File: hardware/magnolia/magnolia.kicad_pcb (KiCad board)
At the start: 4 copper layers, 70.7 x 53.3 mm, 7 parts, among them J1 NEIGHBOR1, J2 NEIGHBOR2, J7 BONUS_ROW

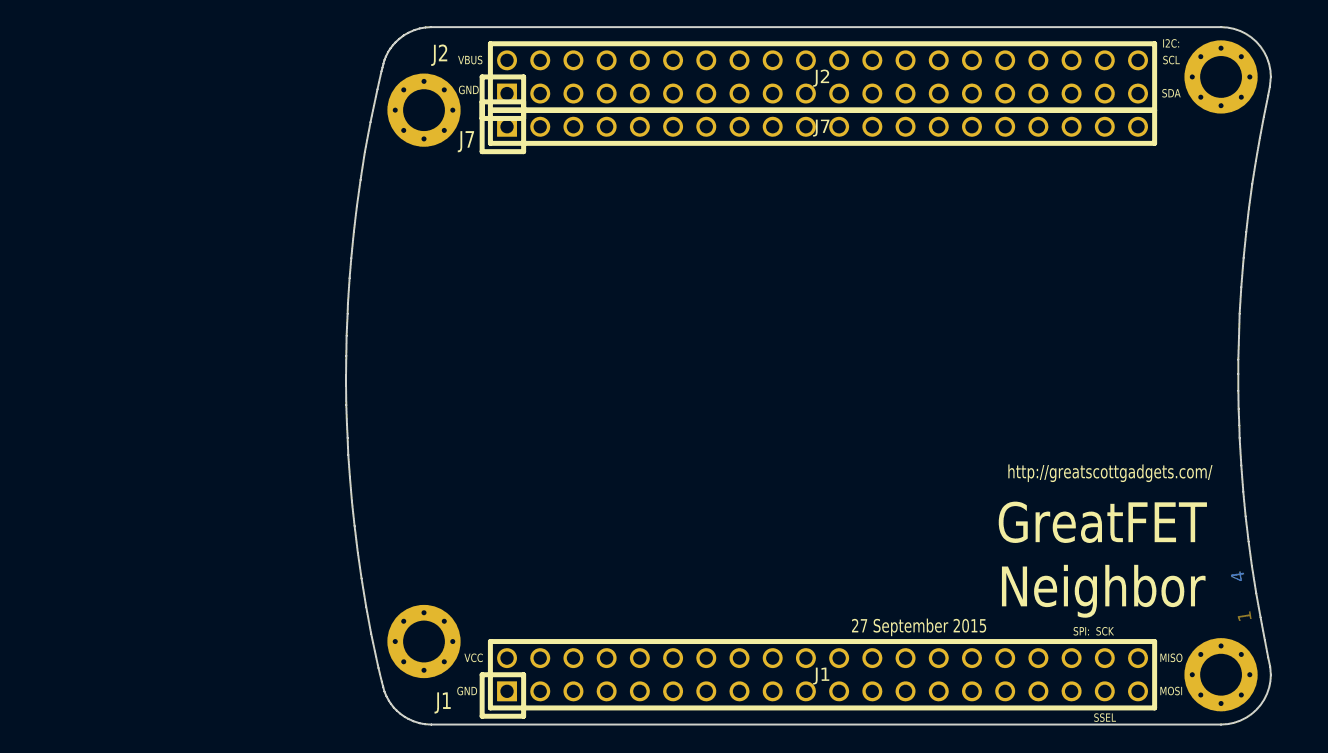
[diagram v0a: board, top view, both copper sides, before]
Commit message: magnolia: route more of Magnolia
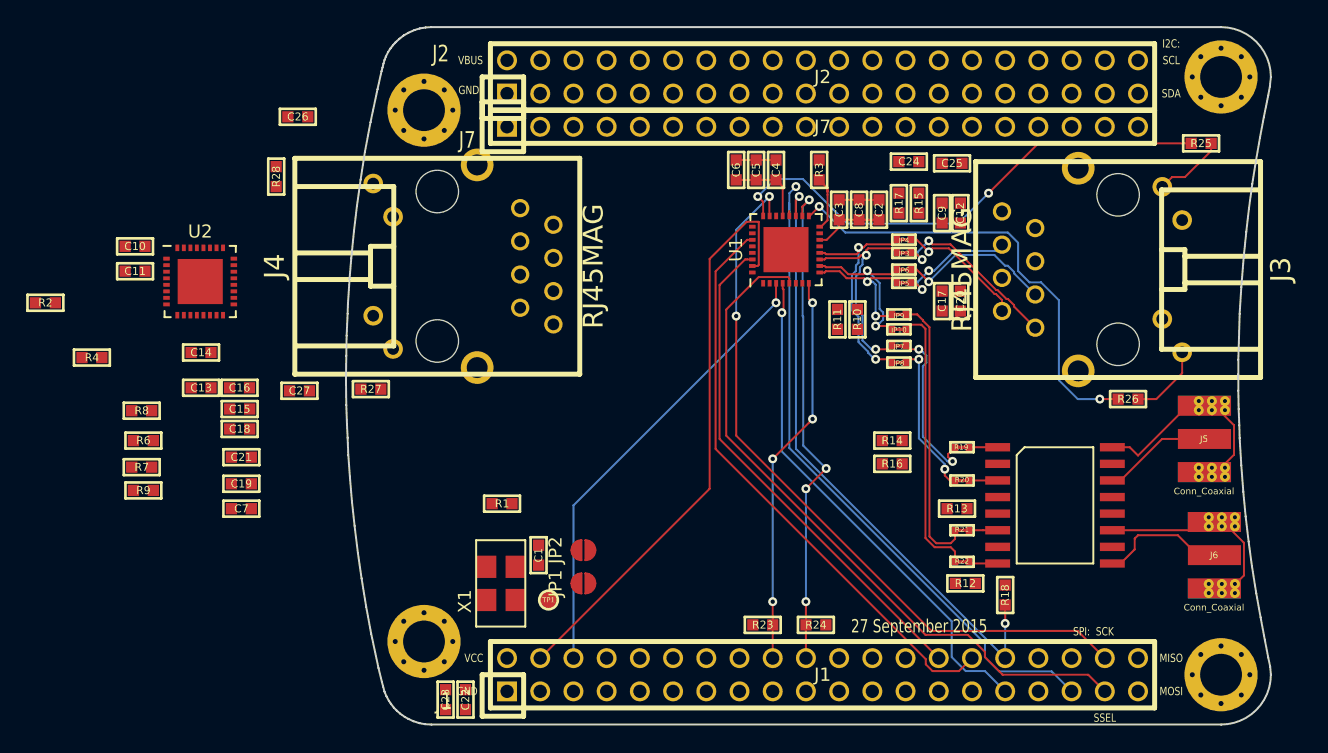
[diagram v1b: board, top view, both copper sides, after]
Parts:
- added C1: 10nF, gsg-modules:0603, F.Cu at (124.3, 109.0)
- added C10: 100nF, gsg-modules:0603, F.Cu at (93.5, 85.3)
- added C11: 1uF, gsg-modules:0603, F.Cu at (93.5, 87.2)
- added C12: 0.1uF, gsg-modules:0603, F.Cu at (156.6, 82.8)
- added C13: 10nF, gsg-modules:0603, F.Cu at (98.5, 96.2)
- added C14: 0.1uF, gsg-modules:0603, F.Cu at (98.5, 93.5)
- added C15: 1uF, gsg-modules:0603, F.Cu at (101.5, 97.8)
- added C16: 100nF, gsg-modules:0603, F.Cu at (101.5, 96.2)
- added C17: 1uF, gsg-modules:0603, F.Cu at (155.2, 89.5)
- added C18: 1uF, gsg-modules:0603, F.Cu at (101.5, 99.3)
- added C19: 1uF, gsg-modules:0603, F.Cu at (101.6, 103.5)
- added C2: 10nF, gsg-modules:0603, F.Cu at (150.4, 82.5)
- added C20: 0.1uF, gsg-modules:0603, F.Cu at (156.6, 89.5)
- added C21: 0.1uF, gsg-modules:0603, F.Cu at (101.6, 101.5)
- added C22: CP, gsg-modules:0603, F.Cu at (118.7, 120.0)
- added C23: CP, gsg-modules:0603, F.Cu at (117.2, 120.0)
- added C24: 100nF, gsg-modules:0603, F.Cu at (152.7, 78.9)
- added C25: 100nF, gsg-modules:0603, F.Cu at (156.0, 79.0)
- added C26: 100nF, gsg-modules:0603, F.Cu at (105.9, 75.4)
- added C27: 100nF, gsg-modules:0603, F.Cu at (106.0, 96.4)
- added C3: 100nF, gsg-modules:0603, F.Cu at (147.3, 82.5)
- added C4: 10nF, gsg-modules:0603, F.Cu at (142.5, 79.5)
- added C5: 1uF, gsg-modules:0603, F.Cu at (141.0, 79.5)
- added C6: 100nF, gsg-modules:0603, F.Cu at (139.4, 79.5)
- added C7: 10nF, gsg-modules:0603, F.Cu at (101.6, 105.4)
- added C8: 1uF, gsg-modules:0603, F.Cu at (148.8, 82.5)
- added C9: 1uF, gsg-modules:0603, F.Cu at (155.2, 82.8)
- added J3: RJ45MAG, gsg-modules:rj45-wiznet-rb1-125bag1a, F.Cu at (168.7, 87.1)
- added J4: RJ45MAG, gsg-modules:rj45-wiznet-rb1-125bag1a, F.Cu at (116.6, 86.9)
- added J5: Conn_Coaxial, gsg-modules:SMA-EDGE, F.Cu at (173.2, 100.1)
- added J6: Conn_Coaxial, gsg-modules:SMA-EDGE, F.Cu at (174.0, 109.0)
- added JP1: Jumper, conn-test:JUMPER-SOLDER-SMD, F.Cu at (127.8, 111.1)
- added JP10: Jumper_NC_Small, gsg-modules:0402-SHORT-10MIL, F.Cu at (151.9, 91.7)
- added JP2: Jumper, conn-test:JUMPER-SOLDER-SMD, F.Cu at (127.8, 108.6)
- added JP3: Jumper_NC_Small, gsg-modules:0402-SHORT-10MIL, F.Cu at (152.3, 85.9)
- added JP4: Jumper_NC_Small, gsg-modules:0402-SHORT-10MIL, F.Cu at (152.3, 84.8)
- added JP5: Jumper_NC_Small, gsg-modules:0402-SHORT-10MIL, F.Cu at (152.3, 88.1)
- added JP6: Jumper_NC_Small, gsg-modules:0402-SHORT-10MIL, F.Cu at (152.3, 87.1)
- added JP7: Jumper_NC_Small, gsg-modules:0402-SHORT-10MIL, F.Cu at (151.9, 93.0)
- added JP8: Jumper_NC_Small, gsg-modules:0402-SHORT-10MIL, F.Cu at (151.9, 94.2)
- added JP9: Jumper_NC_Small, gsg-modules:0402-SHORT-10MIL, F.Cu at (151.9, 90.6)
- added R1: 10K, gsg-modules:0603, F.Cu at (121.5, 105.0)
- added R10: 49R9, gsg-modules:0603, F.Cu at (148.7, 90.9)
- added R11: 49R9, gsg-modules:0603, F.Cu at (147.2, 90.9)
- added R12: 0R, gsg-modules:0603, F.Cu at (157.0, 111.1)
- added R13: 0R, gsg-modules:0603, F.Cu at (156.3, 105.4)
- added R14: 0R, gsg-modules:0603, F.Cu at (151.4, 100.2)
- added R15: 49R9, gsg-modules:0603, F.Cu at (153.4, 82.0)
- added R16: 0R, gsg-modules:0603, F.Cu at (151.4, 102.0)
- added R17: 49R9, gsg-modules:0603, F.Cu at (151.9, 82.0)
- added R18: 2K2, gsg-modules:0603, F.Cu at (160.0, 112.0)
- added R19: R-SHORTED, gsg-modules:0402-SHORT-10MIL, F.Cu at (156.7, 100.7)
- added R2: 2K49, gsg-modules:0603, F.Cu at (86.6, 89.7)
- added R20: R-SHORTED, gsg-modules:0402-SHORT-10MIL, F.Cu at (156.7, 103.3)
- added R21: R-SHORTED, gsg-modules:0402-SHORT-10MIL, F.Cu at (156.7, 107.1)
- added R22: R-SHORTED, gsg-modules:0402-SHORT-10MIL, F.Cu at (156.7, 109.5)
- added R23: 10K, gsg-modules:0603, F.Cu at (141.5, 114.3)
- added R24: 10K, gsg-modules:0603, F.Cu at (145.5, 114.3)
- added R25: 1K, gsg-modules:0603, F.Cu at (175.0, 77.5)
- added R26: 1K, gsg-modules:0603, F.Cu at (169.4, 97.0)
- added R27: 1K, gsg-modules:0603, F.Cu at (111.5, 96.3)
- added R28: 1K, gsg-modules:0603, F.Cu at (104.3, 80.0)
- added R3: 4K87 +/- 1%, gsg-modules:0603, F.Cu at (145.8, 79.5)
- added R4: 4K87 +/- 1%, gsg-modules:0603, F.Cu at (90.2, 93.9)
- added R6: 49R9, gsg-modules:0603, F.Cu at (94.1, 100.2)
- added R7: 49R9, gsg-modules:0603, F.Cu at (94.0, 102.2)
- added R8: 49R9, gsg-modules:0603, F.Cu at (94.0, 97.9)
- added R9: 49R9, gsg-modules:0603, F.Cu at (94.1, 104.0)
- added T1: 749010012A, gsg-modules:749010012A, F.Cu at (163.8, 105.2)
- added TP1: Test_Point, gsg-modules:TESTPOINT-50MIL, F.Cu at (125.1, 112.4)
- added U1: DP83822, gsg-modules:QFN-32_EP_5.15x5.15_Pitch0.5mm, F.Cu at (143.3, 85.6)
- added U2: DP83822, gsg-modules:QFN-32_EP_5.15x5.15_Pitch0.5mm, F.Cu at (98.5, 88.0)
- added X1: ASFL1, gsg-modules:ASFL1, F.Cu at (122.6, 109.9)
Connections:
- net VCC renamed +3V3
- J1 pad 10: (no net) -> /P1_1
- J1 pad 11: (no net) -> /CLK0
- J1 pad 12: (no net) -> /P1_2
- J1 pad 13: (no net) -> /P1_5
- J1 pad 14: (no net) -> /P5_2
- J1 pad 15: (no net) -> /P1_7
- J1 pad 16: (no net) -> /P1_6
- J1 pad 17: (no net) -> /P1_9
- J1 pad 18: (no net) -> /INT_PWDN
- J1 pad 19: (no net) -> /P5_3
- J1 pad 20: (no net) -> /PHY_RESET
- J1 pad 21: (no net) -> /P1_12
- J1 pad 22: (no net) -> /P1_11
- J1 pad 23: (no net) -> /P5_5
- J1 pad 24: (no net) -> /P5_4
- J1 pad 25: (no net) -> /P1_14
- J1 pad 26: (no net) -> /P1_13
- J1 pad 27: (no net) -> /P5_6
- J1 pad 28: (no net) -> /MII_RX_D0
- J1 pad 29: (no net) -> /P5_7
- J1 pad 3: (no net) -> /P4_9
- J1 pad 30: (no net) -> /MII_CRS_DV
- J1 pad 31: (no net) -> /MII_TX_D0
- J1 pad 32: (no net) -> /SMI_MDIO
- J1 pad 33: (no net) -> /P9_5
- J1 pad 34: (no net) -> /P9_6
- J1 pad 35: (no net) -> /SMI_MDC
- J1 pad 36: (no net) -> /P6_0
- J1 pad 37: (no net) -> /MII_TX_D1
- J1 pad 38: (no net) -> /ENET1_RMII_CLK
- J1 pad 39: (no net) -> /P1_4
- J1 pad 4: (no net) -> /MII_RX_D1
- J1 pad 40: (no net) -> /P1_3
- J1 pad 5: (no net) -> /P4_10
- J1 pad 6: (no net) -> /MII_TX_EN
- J1 pad 7: (no net) -> /P1_0
- J1 pad 8: (no net) -> /P5_0
- J1 pad 9: (no net) -> /P5_1
- J2 pad 10: (no net) -> /P4_6
- J2 pad 11: (no net) -> /P4_7
- J2 pad 12: (no net) -> /CLK2
- J2 pad 13: (no net) -> /P2_8
- J2 pad 14: (no net) -> /P2_7
- J2 pad 15: (no net) -> /SGPIO_TX_D0
- J2 pad 16: (no net) -> /P7_7
- J2 pad 17: (no net) -> /WAKEUP0
- J2 pad 18: (no net) -> /P2_5
- J2 pad 19: (no net) -> /P2_4
- J2 pad 20: (no net) -> /P2_3
- J2 pad 21: (no net) -> /PF_4
- J2 pad 22: (no net) -> /P3_2
- J2 pad 23: (no net) -> /P7_2
- J2 pad 24: (no net) -> /P3_1
- J2 pad 25: (no net) -> /P7_1
- J2 pad 26: (no net) -> /P3_0
- J2 pad 27: (no net) -> /P7_0
- J2 pad 28: (no net) -> /P3_4
- J2 pad 29: (no net) -> /P6_8
- J2 pad 3: (no net) -> Net-(J2-Pad3)
- J2 pad 30: (no net) -> /P3_7
- J2 pad 31: (no net) -> /P6_7
- J2 pad 32: (no net) -> /P3_3
- J2 pad 33: (no net) -> /SGPIO_TX_EN
- J2 pad 34: (no net) -> /P6_6
- J2 pad 35: (no net) -> /P2_1
- J2 pad 36: (no net) -> /P6_3
- J2 pad 37: (no net) -> /P3_5
- J2 pad 38: (no net) -> /P3_6
- J2 pad 39: (no net) -> /I2C0_SDA
- J2 pad 4: (no net) -> Net-(J2-Pad4)
- J2 pad 40: (no net) -> /I2C0_SCL
- J2 pad 5: (no net) -> /ADC0_0
- J2 pad 6: (no net) -> /SGPIO_CRS_DV
- J2 pad 7: (no net) -> /SGPIO_TX_D1
- J2 pad 8: (no net) -> /SGPIO_RX_D0
- J2 pad 9: (no net) -> /SGPIO_RX_D1
- J7 pad 11: (no net) -> /RESET
- J7 pad 12: (no net) -> /VBAT
- J7 pad 13: (no net) -> /P2_11
- J7 pad 14: (no net) -> /P2_10
- J7 pad 15: (no net) -> /P6_10
- J7 pad 16: (no net) -> /P6_9
- J7 pad 17: (no net) -> /P6_2
- J7 pad 18: (no net) -> /P6_1
- J7 pad 2: (no net) -> /P6_4
- J7 pad 3: (no net) -> /P6_5
- J7 pad 4: (no net) -> /ADC0_5
- J7 pad 5: (no net) -> /ADC0_2
- J7 pad 6: (no net) -> /P2_9
- J7 pad 7: (no net) -> /P2_12
- J7 pad 8: (no net) -> /P2_13
- J7 pad 9: (no net) -> /RTC_ALARM
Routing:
- net /ENET1_RMII_CLK: track 0.00 -> 56.1 mm, vias 0 -> 2
- net /MII_TX_D1: track 0.00 -> 53.2 mm
- net /SMI_MDC: track 0.00 -> 51.5 mm, vias 0 -> 1
- net /SMI_MDIO: track 0.00 -> 47.7 mm, vias 0 -> 2
- net /MII_CRS_DV: track 0.00 -> 44.7 mm
- net /MII_RX_D1: track 0.00 -> 44.6 mm
- net Net-(R25-Pad2): track 0.00 -> 39.3 mm, vias 0 -> 2
- net /MII_TX_D0: track 0.00 -> 39.2 mm, vias 0 -> 1
- net /MII_RX_D0: track 0.00 -> 38.8 mm
- net /PHY_RESET: track 0.00 -> 38.1 mm, vias 0 -> 4
- net /MII_TX_EN: track 0.00 -> 35.1 mm, vias 0 -> 1
- net Net-(R26-Pad2): track 0.00 -> 34.9 mm, vias 0 -> 2
- net /INT_PWDN: track 0.00 -> 30.0 mm, vias 0 -> 4
- net /TDR1_RD_P: track 0.00 -> 20.9 mm
- net /TDR1_RD_N: track 0.00 -> 20.8 mm
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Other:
- net class Default: trace_width 0.2032 -> 0.1524; via_dia 0.762 -> 0.6858
- rule trace_min: 0.2032 -> 0.1524
- rule via_min_drill: 0.3302 -> 0.254
- rule via_min_size: 0.6858 -> 0.508
- board text removed: "1"
- board text removed: "2"
- board text removed: "3"
- board text removed: "4"
- board text removed: "GreatFET Neighbor"
- board text removed: "http://greatscottgadgets.com/"

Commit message: magnolia: route more
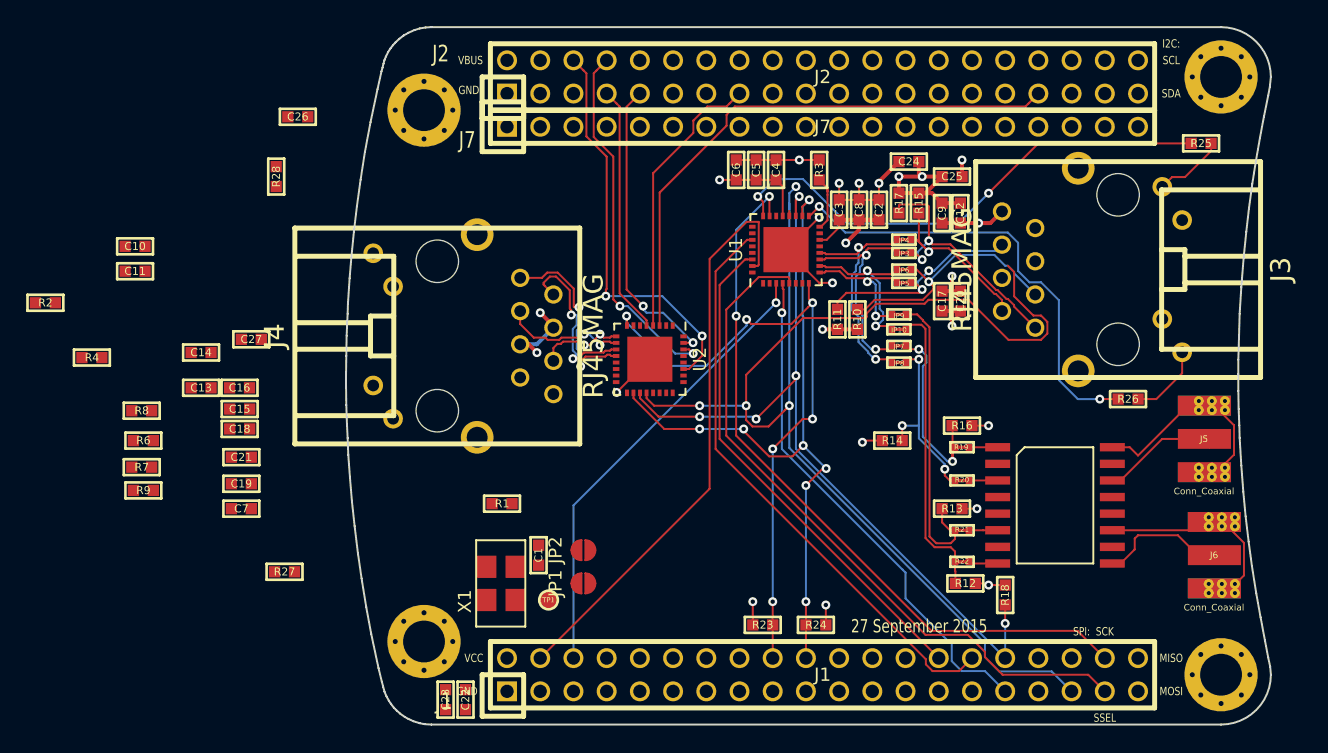
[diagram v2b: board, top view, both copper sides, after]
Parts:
- moved U2 34.9 mm to (132.8, 94.0), turned to 270 degrees
- moved R27 15.5 mm to (104.9, 110.2)
- moved R16 6.08 mm to (156.7, 99.1), turned to 180 degrees
- moved C27 5.39 mm to (102.4, 92.5)
- moved J4 5.33 mm to (116.6, 92.2)
- moved C25 1.02 mm to (156.0, 80.0), turned to 180 degrees
- moved R13 0.38 mm to (156.0, 105.4)
- turned C9 to 270 degrees
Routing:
- net /SMI_MDC: track 51.5 -> 101.2 mm, vias 1 -> 4
- net /SGPIO_TX_EN: track 0.00 -> 42.8 mm
- net +3V3: track 11.5 -> 52.2 mm, vias 0 -> 14
- net GND: track 13.3 -> 46.7 mm, vias 0 -> 10
- net /SGPIO_CRS_DV: track 0.00 -> 31.1 mm, vias 0 -> 2
- net /SGPIO_RX_D0: track 0.00 -> 28.0 mm, vias 0 -> 2
- net /SGPIO_RX_D1: track 0.00 -> 23.1 mm, vias 0 -> 2
- net /SGPIO_TX_D0: track 0.00 -> 21.3 mm
- net /INT_PWDN: track 30.0 -> 49.9 mm, vias 4 -> 6
- net /SGPIO_TX_D1: track 0.00 -> 19.0 mm
- net /PHY_RESET: track 38.1 -> 53.7 mm, vias 4 -> 7
- net /ENET2_TD_P: track 0.00 -> 14.9 mm, vias 0 -> 2
- net /SMI_MDIO: track 47.7 -> 62.2 mm, vias 2 -> 5
- net /ENET2_TD_N: track 0.00 -> 13.5 mm, vias 0 -> 2
- net /ENET2_RD_P: track 0.00 -> 9.51 mm, vias 0 -> 2
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
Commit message: magnolia: check in completed (but never cheked in) r0 PCB
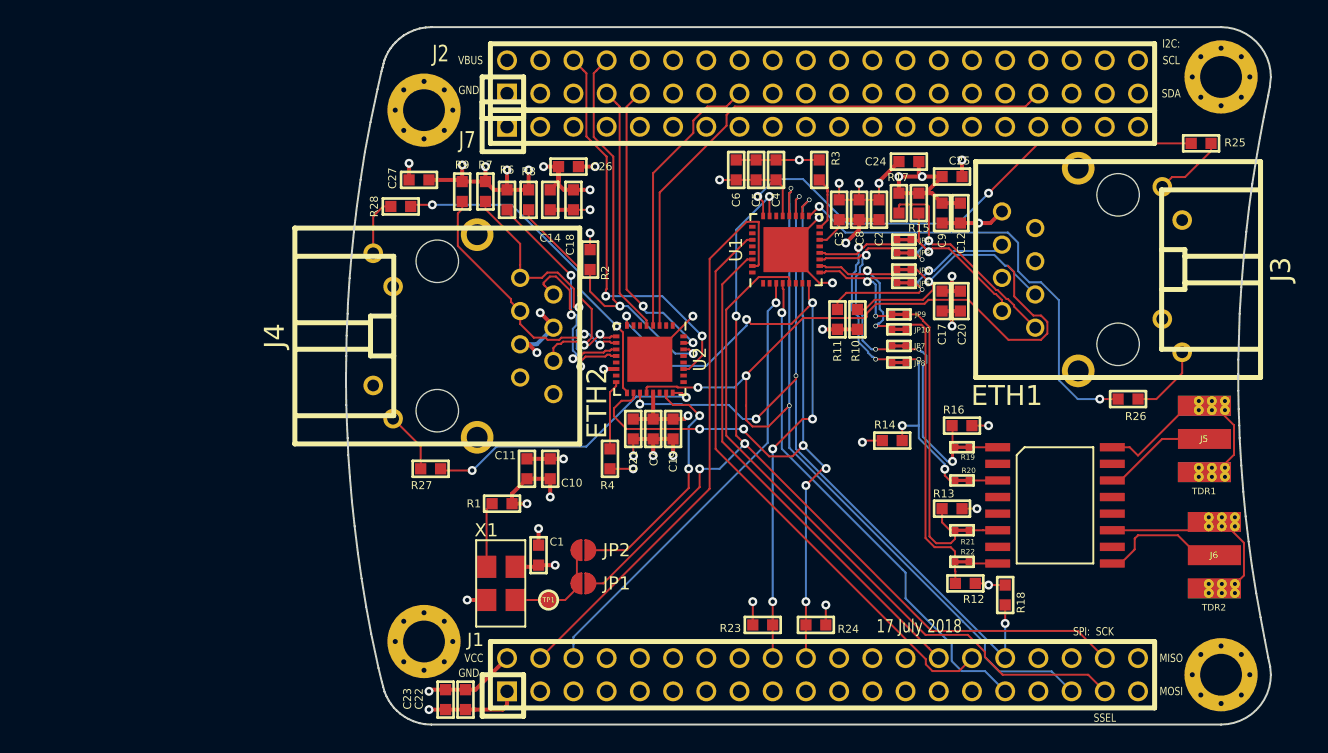
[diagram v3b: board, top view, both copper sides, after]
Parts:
- removed C13: 10nF, gsg-modules:0603
- removed C15: 1uF, gsg-modules:0603
- removed C16: 100nF, gsg-modules:0603
- J3: value RJ45MAG -> ETH1
- J4: value RJ45MAG -> ETH2
- J5: value Conn_Coaxial -> TDR1
- J6: value Conn_Coaxial -> TDR2
- moved R2 41.8 mm to (128.3, 86.4), turned to 270 degrees
- moved R4 40.4 mm to (129.8, 101.6), turned to 90 degrees
- moved C10 36.0 mm to (125.2, 102.4), turned to 90 degrees
- moved R8 33.7 mm to (123.6, 81.8), turned to 270 degrees
- moved R7 33.7 mm to (120.3, 81.2), turned to 270 degrees
- moved C11 33.6 mm to (123.4, 102.4), turned to 90 degrees
- moved R9 33.4 mm to (118.5, 81.2), turned to 270 degrees
- moved R6 33.4 mm to (121.9, 81.8), turned to 270 degrees
- moved C19 33.3 mm to (134.6, 99.3), turned to 270 degrees
- moved C7 32.1 mm to (133.1, 99.3), turned to 270 degrees
- moved C18 31.0 mm to (127.0, 81.8), turned to 90 degrees
- moved C21 30.0 mm to (131.6, 99.3), turned to 270 degrees
- moved C14 29.1 mm to (125.2, 81.8), turned to 90 degrees
- moved C26 21.0 mm to (126.6, 79.2)
- moved C27 17.7 mm to (115.2, 80.3)
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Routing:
- net +3V3: track 52.2 -> 95.3 mm, vias 14 -> 27
- net GND: track 46.7 -> 77.5 mm, vias 10 -> 21
- net Net-(R28-Pad2): track 0.00 -> 25.8 mm, vias 0 -> 2
- net Net-(R27-Pad2): track 0.00 -> 22.4 mm, vias 0 -> 2
- net /ENET2_RMII_CLK: track 0.00 -> 18.9 mm, vias 0 -> 2
- net /ENET1_RMII_CLK: track 56.1 -> 73.2 mm, vias 2 -> 4
- net /ENET2_RD_N: track 6.30 -> 18.9 mm
- net /ENET2_RD_P: track 9.51 -> 20.0 mm
- net /ENET2_TD_N: track 13.5 -> 23.6 mm, vias 2 -> 3
- net Net-(JP1-Pad1): track 0.00 -> 7.99 mm
- net /ENET2_TD_P: track 14.9 -> 21.8 mm
- net /REF_CLK_ENABLE: track 0.00 -> 5.60 mm
- net Net-(R4-Pad2): track 0.00 -> 5.30 mm
- net Net-(J4-Pad9): track 0.00 -> 4.71 mm
- net Net-(J4-Pad12): track 0.00 -> 4.48 mm
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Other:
- net class Default: clearance 0.1524 -> 0.127; via_dia 0.6858 -> 0.3556; via_drill 0.3302 -> 0.254
- rule trace_clearance: 0.1524 -> 0.127
- rule trace_min: 0.1524 -> 0.127
- rule via_min_size: 0.508 -> 0.3556
- board text added: "17 July 2018"
- board text removed: "27 September 2015"
- board text removed: "J1"
